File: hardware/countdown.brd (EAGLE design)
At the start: 38 x 40 mm, 30 parts, among them J1 BURNIN, J2 USB, J3 LiPo, J4 OLED, J5 TOP, J6 BASE, U1 DS3231MZ+TRL_SOIC8, U2 ATMEGA328P-AUR, U3 MCP73831T, U4 BL1551

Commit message: jlc order done
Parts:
- added C8: 0.1uF, scono:0402-CAP
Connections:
- net GND_TOP: now also C8.1
- net INT_WAKE: now also C8.2
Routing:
- net INT_WAKE: track 8.00 -> 10.7 mm
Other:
- outline, holes or cut-outs redrawn
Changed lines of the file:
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@@
 <layer number="25" name="tNames" color="7" fill="1" visible="yes" active="yes"/>
 <layer number="26" name="bNames" color="7" fill="1" visible="yes" active="yes"/>
-<layer number="27" name="tValues" color="7" fill="1" visible="yes" active="yes"/>
+<layer number="27" name="tValues" color="7" fill="1" visible="no" active="yes"/>
 <layer number="28" name="bValues" color="7" fill="1" visible="no" active="yes"/>
-<layer number="29" name="tStop" color="7" fill="3" visible="yes" active="yes"/>
-<layer number="30" name="bStop" color="7" fill="6" visible="yes" active="yes"/>
-<layer number="31" name="tCream" color="7" fill="4" visible="yes" active="yes"/>
+<layer number="29" name="tStop" color="7" fill="3" visible="no" active="yes"/>
+<layer number="30" name="bStop" color="7" fill="6" visible="no" active="yes"/>
+<layer number="31" name="tCream" color="7" fill="4" visible="no" active="yes"/>
 <layer number="32" name="bCream" color="7" fill="5" visible="no" active="yes"/>
 <layer number="33" name="tFinish" color="6" fill="3" visible="no" active="yes"/>
 <layer number="34" name="bFinish" color="6" fill="6" visible="no" active="yes"/>
-<layer number="35" name="tGlue" color="7" fill="4" visible="yes" active="yes"/>
+<layer number="35" name="tGlue" color="7" fill="4" visible="no" active="yes"/>
 <layer number="36" name="bGlue" color="7" fill="5" visible="no" active="yes"/>
 <layer number="37" name="tTest" color="7" fill="1" visible="no" active="yes"/>
@@
 <layer number="42" name="bRestrict" color="1" fill="10" visible="yes" active="yes"/>
 <layer number="43" name="vRestrict" color="2" fill="10" visible="no" active="yes"/>
-<layer number="44" name="Drills" color="7" fill="1" visible="yes" active="yes"/>
-<layer number="45" name="Holes" color="7" fill="1" visible="yes" active="yes"/>
-<layer number="46" name="Milling" color="3" fill="1" visible="yes" active="yes"/>
+<layer number="44" name="Drills" color="7" fill="1" visible="no" active="yes"/>
+<layer number="45" name="Holes" color="7" fill="1" visible="no" active="yes"/>
+<layer number="46" name="Milling" color="3" fill="1" visible="no" active="yes"/>
 <layer number="47" name="Measures" color="7" fill="1" visible="yes" active="yes"/>
-<layer number="48" name="Document" color="7" fill="1" visible="yes" active="yes"/>
+<layer number="48" name="Document" color="7" fill="1" visible="no" active="yes"/>
 <layer number="49" name="Reference" color="7" fill="1" visible="yes" active="yes"/>
 <layer number="50" name="dxf" color="7" fill="1" visible="no" active="no"/>
@@
 <layer number="110" name="fp0" color="7" fill="1" visible="no" active="yes"/>
 <layer number="111" name="LPC17xx" color="7" fill="1" visible="no" active="yes"/>
-<layer number="112" name="tSilk" color="7" fill="1" visible="yes" active="yes"/>
+<layer number="112" name="tSilk" color="7" fill="1" visible="no" active="yes"/>
 <layer number="113" name="IDFDebug" color="7" fill="1" visible="no" active="yes"/>
 <layer number="114" name="Badge_Outline" color="11" fill="1" visible="no" active="no"/>
@@
 <wire x1="36" y1="40" x2="38" y2="38" width="0" layer="20" curve="-90"/>
 <wire x1="38" y1="30" x2="36" y2="28" width="0" layer="20" curve="-90"/>
-<wire x1="38" y1="21" x2="38" y2="2.25" width="0" layer="20"/>
-<wire x1="35.75" y1="0" x2="1.75" y2="0" width="0" layer="20"/>
-<wire x1="0" y1="2.25" x2="0" y2="21" width="0" layer="20"/>
-<wire x1="1.75" y1="0" x2="0" y2="2.25" width="0" layer="20" curve="-90"/>
+<wire x1="38" y1="21" x2="38" y2="2" width="0" layer="20"/>
+<wire x1="36" y1="0" x2="2" y2="0" width="0" layer="20"/>
+<wire x1="0" y1="2" x2="0" y2="21" width="0" layer="20"/>
+<wire x1="2" y1="0" x2="0" y2="2" width="0" layer="20" curve="-90"/>
 <wire x1="0" y1="21" x2="2" y2="23" width="0" layer="20" curve="-90"/>
 <wire x1="36" y1="23" x2="38" y2="21" width="0" layer="20" curve="-90"/>
-<wire x1="38" y1="2.25" x2="35.75" y2="0" width="0" layer="20" curve="-90"/>
+<wire x1="38" y1="2" x2="36" y2="0" width="0" layer="20" curve="-90"/>
 <wire x1="36" y1="28" x2="35" y2="28" width="0" layer="20"/>
 <wire x1="36" y1="23" x2="35" y2="23" width="0" layer="20"/>
@@
 </element>
 <element name="R6" library="scono" library_urn="urn:adsk.eagle:library:14850048" package="R0402" package3d_urn="urn:adsk.eagle:package:14850590/3" value="10k" x="5" y="35.5" smashed="yes" rot="R90">
-<attribute name="NAME" x="4.238" y="34.357" size="0.508" layer="25" font="vector" ratio="10" rot="R90"/>
 <attribute name="VALUE" x="6.27" y="34.357" size="0.508" layer="27" font="vector" rot="R90"/>
 </element>
@@
 <element name="R7" library="scono" library_urn="urn:adsk.eagle:library:14850048" package="R0402" package3d_urn="urn:adsk.eagle:package:14850590/3" value="330R" x="17" y="7.75" smashed="yes" rot="R180">
 <attribute name="VALUE" x="18.143" y="9.02" size="0.508" layer="27" font="vector" rot="R180"/>
+</element>
+<element name="C8" library="scono" library_urn="urn:adsk.eagle:library:14850048" package="0402-CAP" package3d_urn="urn:adsk.eagle:package:14850678/3" value="0.1uF" x="2.25" y="29.5" smashed="yes" rot="R180">
+<attribute name="PIE-INT-REF-NUM" value="CAPACITOR-GENERIC" x="2.25" y="29.5" size="1.778" layer="27" rot="R180" display="off"/>
 </element>
 </elements>
@@
 <wire x1="32.5" y1="33.25" x2="34.5" y2="31.25" width="0.1524" layer="16"/>
 <wire x1="34.5" y1="31.25" x2="36.5" y2="31.25" width="0.1524" layer="16"/>
-<wire x1="37" y1="31.75" x2="37" y2="36.5" width="0.1524" layer="16"/>
-<wire x1="37" y1="36.5" x2="35.88" y2="37.62" width="0.1524" layer="16"/>
+<wire x1="36.75" y1="31.5" x2="36.75" y2="36.75" width="0.1524" layer="16"/>
+<wire x1="36.75" y1="36.75" x2="35.88" y2="37.62" width="0.1524" layer="16"/>
 <wire x1="35.88" y1="37.62" x2="35.5" y2="37.62" width="0.1524" layer="16"/>
-<wire x1="36.5" y1="31.25" x2="37" y2="31.75" width="0.1524" layer="16"/>
+<wire x1="36.5" y1="31.25" x2="36.75" y2="31.5" width="0.1524" layer="16"/>
 <wire x1="12.2" y1="37.93" x2="12.2" y2="36.7" width="0.1524" layer="1"/>
 <wire x1="12.2" y1="36.7" x2="11.75" y2="36.25" width="0.1524" layer="1"/>
@@
 <wire x1="8.25" y1="35" x2="8.2" y2="34.95" width="0.1524" layer="1"/>
 <wire x1="8.2" y1="34.95" x2="6.82" y2="34.95" width="0.1524" layer="1"/>
+<contactref element="C8" pad="1"/>
 </signal>
 <signal name="V_BAT_TOP">
@@
 <wire x1="5" y1="36.15" x2="5.4" y2="36.55" width="0.1524" layer="1"/>
 <wire x1="5.4" y1="36.55" x2="6.82" y2="36.55" width="0.1524" layer="1"/>
+<contactref element="C8" pad="2"/>
+<wire x1="2.02" y1="32.035" x2="2.02" y2="29.92" width="0.1524" layer="1"/>
+<wire x1="2.02" y1="29.92" x2="1.6" y2="29.5" width="0.1524" layer="1"/>
 </signal>
 <signal name="N$2">

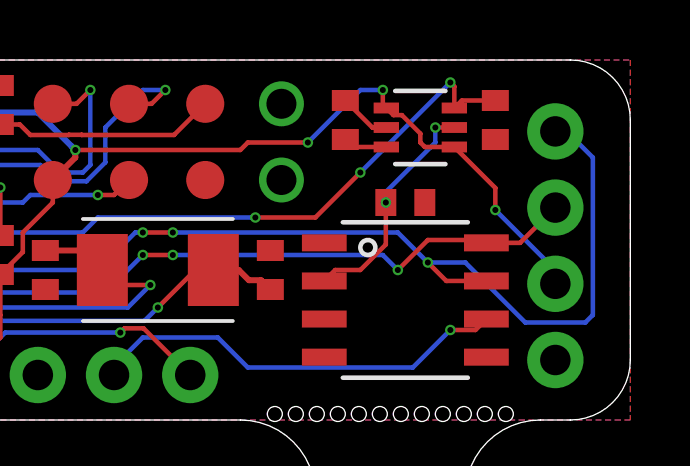
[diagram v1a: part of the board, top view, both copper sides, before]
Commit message: small fixes to board from debugging
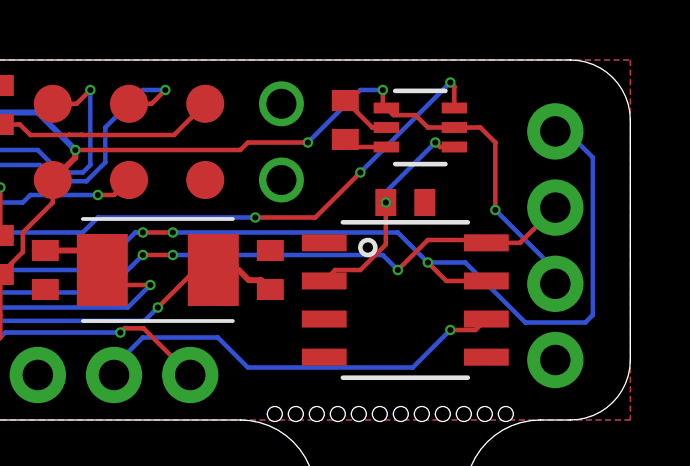
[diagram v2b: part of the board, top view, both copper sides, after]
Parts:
- removed R4: 10k, scono:R0402
- R3: value 1k -> 10k
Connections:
- net EN_CLK: no longer R4.1
- net GND_TOP: no longer R4.2
- net VCC_CLK: now also U4.4; no longer U4.5
- net VCC_TOP: now also U4.5; no longer U4.4
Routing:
- net EN_CLK: track 27.1 -> 25.6 mm
- net VCC_TOP: track 73.3 -> 74.0 mm
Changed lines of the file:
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@@
 <element name="R1" library="scono" library_urn="urn:adsk.eagle:library:14850048" package="R0402" package3d_urn="urn:adsk.eagle:package:14850590/3" value="330R" x="15.25" y="2.75" smashed="yes" rot="R180"/>
 <element name="R2" library="scono" library_urn="urn:adsk.eagle:library:14850048" package="R0402" package3d_urn="urn:adsk.eagle:package:14850590/3" value="51k" x="12" y="7.75" smashed="yes" rot="R180"/>
-<element name="R3" library="scono" library_urn="urn:adsk.eagle:library:14850048" package="R0402" package3d_urn="urn:adsk.eagle:package:14850590/3" value="1k" x="17" y="38.5" smashed="yes" rot="R270"/>
+<element name="R3" library="scono" library_urn="urn:adsk.eagle:library:14850048" package="R0402" package3d_urn="urn:adsk.eagle:package:14850590/3" value="10k" x="17" y="38.5" smashed="yes" rot="R270"/>
 <element name="U$1" library="scono" library_urn="urn:adsk.eagle:library:14850048" package="12C-12" value="CL-SB-12C-12" x="31.5" y="3.75" smashed="yes" rot="R180"/>
 <element name="U1" library="scono" library_urn="urn:adsk.eagle:library:14850048" package="SOIC-8" package3d_urn="urn:adsk.eagle:package:19765866/1" value="DS3231MZ+TRL_SOIC8" x="30.5" y="32" smashed="yes"/>
@@
 </element>
 <element name="U4" library="scono" library_urn="urn:adsk.eagle:library:14850048" package="SOT-363" value="BL1551" x="31" y="37.75" smashed="yes"/>
-<element name="R4" library="scono" library_urn="urn:adsk.eagle:library:14850048" package="R0402" package3d_urn="urn:adsk.eagle:package:14850590/3" value="10k" x="33.5" y="38" smashed="yes" rot="R270"/>
 <element name="R5" library="scono" library_urn="urn:adsk.eagle:library:14850048" package="R0402" package3d_urn="urn:adsk.eagle:package:14850590/3" value="10k" x="28.5" y="38" smashed="yes" rot="R90"/>
 <element name="J5" library="scono" library_urn="urn:adsk.eagle:library:14850048" package="1X03_NO_SILK" package3d_urn="urn:adsk.eagle:package:38076/1" value="TOP" x="18.25" y="29.5" smashed="yes"/>
@@
 <contactref element="U1" pad="2"/>
 <contactref element="C7" pad="2"/>
-<contactref element="U4" pad="5"/>
 <wire x1="27.797703125" y1="32.635" x2="28.162703125" y2="33" width="0.1524" layer="1"/>
 <wire x1="28.162703125" y1="33" x2="29" y2="33" width="0.1524" layer="1"/>
@@
 <via x="29.85" y="35.25" extent="1-16" drill="0.2"/>
 <wire x1="29.85" y1="35.25" x2="29.85" y2="35.6" width="0.1524" layer="16"/>
-<wire x1="31.5" y1="37.75" x2="32.13385" y2="37.75" width="0.1524" layer="1"/>
-<wire x1="31.5" y1="37.25" x2="31.5" y2="37.75" width="0.1524" layer="16"/>
-<via x="31.5" y="37.75" extent="1-16" drill="0.2"/>
+<via x="31.5" y="37.25" extent="1-16" drill="0.2"/>
 <wire x1="29.85" y1="35.6" x2="31.5" y2="37.25" width="0.1524" layer="16"/>
+<contactref element="U4" pad="4"/>
+<wire x1="32.13385" y1="37.1" x2="31.65" y2="37.1" width="0.1524" layer="1"/>
+<wire x1="31.65" y1="37.1" x2="31.5" y2="37.25" width="0.1524" layer="1"/>
 </signal>
 <signal name="EN_CLK">
 <contactref element="U4" pad="6"/>
 <contactref element="U2" pad="25"/>
-<contactref element="R4" pad="1"/>
-<wire x1="33.5" y1="38.65" x2="32.38385" y2="38.65" width="0.1524" layer="1"/>
-<wire x1="32.38385" y1="38.65" x2="32.13385" y2="38.4" width="0.1524" layer="1"/>
 <wire x1="32.13385" y1="38.4" x2="32.13385" y2="39.11615" width="0.1524" layer="1"/>
 <wire x1="32.13385" y1="39.11615" x2="32" y2="39.25" width="0.1524" layer="1"/>
@@
 <contactref element="R5" pad="2"/>
 <contactref element="U4" pad="2"/>
-<contactref element="R4" pad="2"/>
 <contactref element="C1" pad="1"/>
 <contactref element="C2" pad="1"/>
@@
 <contactref element="U4" pad="1"/>
 <contactref element="J4" pad="2"/>
-<contactref element="U4" pad="4"/>
 <contactref element="R3" pad="1"/>
 <contactref element="U2" pad="4"/>
@@
 <wire x1="5" y1="32.35" x2="5.2" y2="32.55" width="0.1524" layer="1"/>
 <wire x1="5.2" y1="32.55" x2="6.82" y2="32.55" width="0.1524" layer="1"/>
-<wire x1="32.13385" y1="37.1" x2="33.5" y2="35.73385" width="0.1524" layer="1"/>
-<wire x1="33.5" y1="35.73385" x2="33.5" y2="35" width="0.1524" layer="1"/>
 <via x="33.5" y="35" extent="1-16" drill="0.2"/>
 <wire x1="33.5" y1="35" x2="35.5" y2="33" width="0.1524" layer="16"/>
@@
 <via x="29.75" y="39" extent="1-16" drill="0.2"/>
 <wire x1="29.86615" y1="38.4" x2="30.10355" y2="38.1626" width="0.1524" layer="1"/>
-<wire x1="30.10355" y1="38.1626" x2="30.38415" y2="38.1626" width="0.1524" layer="1"/>
-<wire x1="31" y1="37.54675" x2="31" y2="37.25" width="0.1524" layer="1"/>
-<wire x1="31" y1="37.25" x2="31.15" y2="37.1" width="0.1524" layer="1"/>
-<wire x1="31.15" y1="37.1" x2="32.13385" y2="37.1" width="0.1524" layer="1"/>
-<wire x1="30.38415" y1="38.1626" x2="31" y2="37.54675" width="0.1524" layer="1"/>
 <wire x1="25" y1="37" x2="25.25" y2="37.25" width="0.1524" layer="1"/>
 <via x="27.25" y="37.25" extent="1-16" drill="0.2"/>
@@
 <wire x1="16.75" y1="30.5" x2="17" y2="30.75" width="0.1524" layer="1"/>
 <wire x1="17" y1="30.75" x2="17" y2="31.5" width="0.1524" layer="1"/>
+<contactref element="U4" pad="5"/>
+<wire x1="31.25" y1="37.75" x2="32.13385" y2="37.75" width="0.1524" layer="1"/>
+<wire x1="30.10355" y1="38.1626" x2="30.8374" y2="38.1626" width="0.1524" layer="1"/>
+<wire x1="30.8374" y1="38.1626" x2="31.25" y2="37.75" width="0.1524" layer="1"/>
+<wire x1="32.13385" y1="37.75" x2="33" y2="37.75" width="0.1524" layer="1"/>
+<wire x1="33" y1="37.75" x2="33.5" y2="37.25" width="0.1524" layer="1"/>
+<wire x1="33.5" y1="37.25" x2="33.5" y2="35" width="0.1524" layer="1"/>
 </signal>
 <signal name="AREF">
